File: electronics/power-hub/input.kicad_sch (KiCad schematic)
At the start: 30 parts, among them J1 PD IN, Q1 IRF7842TRPBF, Q2 IRF7842TRPBF, U1 AP33772SDKZ-13-FA01

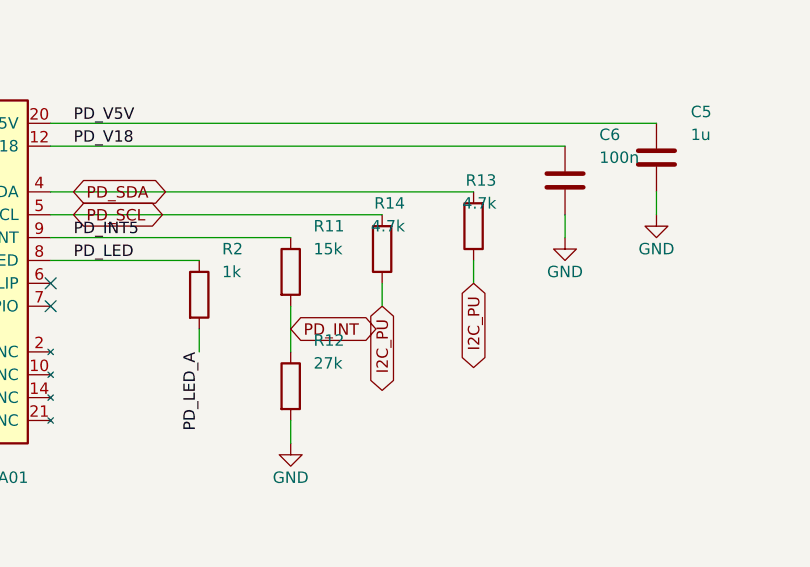
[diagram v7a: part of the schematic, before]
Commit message: Power hub: lead-free HASL and six part types fewer, ≈ $22 off
The user found the hub dear ($242.52 quoted).  JLC's calculator
(2026-10-19, 5 boards, 4 layers) shows where it goes: ENIG $18.00
against lead-free HASL $5.30, and the $25 engineering fee comes from the
length (86 x 100 mm with the rails falls under the 4-layer offer).

- Finish: lead-free HASL, as the node.  It was ENIG for the MINI-1's LGA
  pads; JLC X-rays the module either way.  -$12.70.
- Six resistor values merged onto values the board already has (no
  footprint or track moves): FB 100k/18k (5.24 V, as the node), EN
  39k/18k (on at 3.9 V), PD INT 10k/18k (3.2 V), I2C pull-ups 5.1k.
  Six fewer part types at $1.55 in Standard PCBA's feeders: -$9.30.

Same Freerouting session re-imported (1241 segments, 593 vias): ERC 0,
DRC only the known C8 silkscreen warning, 0 unconnected, parity 0.
tools/bom.py applies both to the quote as adjustments: ≈ $220.52.

Co-Authored-By: Claude Opus 5.5 <noreply@anthropic.com>
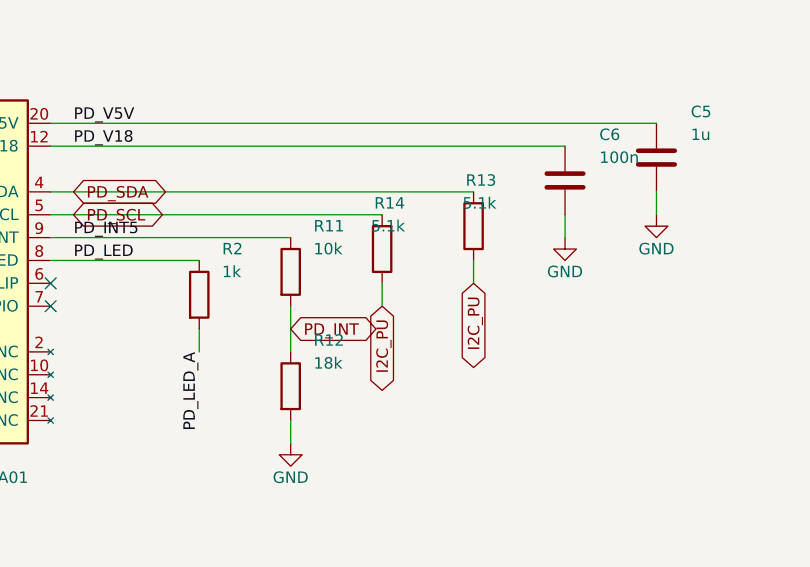
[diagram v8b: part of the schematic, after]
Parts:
- R11: value 15k -> 10k; LCSC C22809 -> C25804; MPN 0603WAF1502T5E -> 0603WAF1002T5E
- R12: value 27k -> 18k; LCSC C22967 -> C25810; MPN 0603WAF2702T5E -> 0603WAF1802T5E
- R13, R14: value 4.7k -> 5.1k; LCSC C23162 -> C23186; MPN 0603WAF4701T5E -> 0603WAF5101T5E
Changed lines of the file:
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@@
 			)
 		)
-		(property "Value" "15k"
+		(property "Value" "10k"
 			(at 180.34 128.27 0)
 			(effects
@@
 			)
 		)
-		(property "Description" "Resistor 15k 0603"
-			(at 177.8 130.81 0)
-			(effects
-				(font
-					(size 1.27 1.27)
-				)
-				(hide yes)
-			)
-		)
-		(property "LCSC" "C22809"
-			(at 177.8 130.81 0)
-			(effects
-				(font
-					(size 1.27 1.27)
-				)
-				(hide yes)
-			)
-		)
-		(property "MPN" "0603WAF1502T5E"
+		(property "Description" "Resistor 10k 0603"
+			(at 177.8 130.81 0)
+			(effects
+				(font
+					(size 1.27 1.27)
+				)
+				(hide yes)
+			)
+		)
+		(property "LCSC" "C25804"
+			(at 177.8 130.81 0)
+			(effects
+				(font
+					(size 1.27 1.27)
+				)
+				(hide yes)
+			)
+		)
+		(property "MPN" "0603WAF1002T5E"
 			(at 177.8 130.81 0)
 			(effects
@@
 			)
 		)
-		(property "Value" "27k"
+		(property "Value" "18k"
 			(at 180.34 140.97 0)
 			(effects
@@
 			)
 		)
-		(property "Description" "Resistor 27k 0603"
-			(at 177.8 143.51 0)
-			(effects
-				(font
-					(size 1.27 1.27)
-				)
-				(hide yes)
-			)
-		)
-		(property "LCSC" "C22967"
-			(at 177.8 143.51 0)
-			(effects
-				(font
-					(size 1.27 1.27)
-				)
-				(hide yes)
-			)
-		)
-		(property "MPN" "0603WAF2702T5E"
+		(property "Description" "Resistor 18k 0603"
+			(at 177.8 143.51 0)
+			(effects
+				(font
+					(size 1.27 1.27)
+				)
+				(hide yes)
+			)
+		)
+		(property "LCSC" "C25810"
+			(at 177.8 143.51 0)
+			(effects
+				(font
+					(size 1.27 1.27)
+				)
+				(hide yes)
+			)
+		)
+		(property "MPN" "0603WAF1802T5E"
 			(at 177.8 143.51 0)
 			(effects
@@
 			)
 		)
-		(property "Value" "4.7k"
+		(property "Value" "5.1k"
 			(at 200.66 123.19 0)
 			(effects
@@
 			)
 		)
-		(property "Description" "Resistor 4.7k 0603"
-			(at 198.12 125.73 0)
-			(effects
-				(font
-					(size 1.27 1.27)
-				)
-				(hide yes)
-			)
-		)
-		(property "LCSC" "C23162"
-			(at 198.12 125.73 0)
-			(effects
-				(font
-					(size 1.27 1.27)
-				)
-				(hide yes)
-			)
-		)
-		(property "MPN" "0603WAF4701T5E"
+		(property "Description" "Resistor 5.1k 0603"
+			(at 198.12 125.73 0)
+			(effects
+				(font
+					(size 1.27 1.27)
+				)
+				(hide yes)
+			)
+		)
+		(property "LCSC" "C23186"
+			(at 198.12 125.73 0)
+			(effects
+				(font
+					(size 1.27 1.27)
+				)
+				(hide yes)
+			)
+		)
+		(property "MPN" "0603WAF5101T5E"
 			(at 198.12 125.73 0)
 			(effects
@@
 			)
 		)
-		(property "Value" "4.7k"
+		(property "Value" "5.1k"
 			(at 190.5 125.73 0)
 			(effects
@@
 			)
 		)
-		(property "Description" "Resistor 4.7k 0603"
+		(property "Description" "Resistor 5.1k 0603"
 			(at 187.96 128.27 0)
 			(effects
@@
 			)
 		)
-		(property "LCSC" "C23162"
+		(property "LCSC" "C23186"
 			(at 187.96 128.27 0)
 			(effects
@@
 			)
 		)
-		(property "MPN" "0603WAF4701T5E"
+		(property "MPN" "0603WAF5101T5E"
 			(at 187.96 128.27 0)
 			(effects
